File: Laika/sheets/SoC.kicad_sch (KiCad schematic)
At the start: 0 parts

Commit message: Connected USB data in schematic, adjusted Project Architecture
Adjusted the Project Architecture sheet and connected USB between the
Power Connector and SoC sheet. Cleaned up look of the Project
Architecture sheet. Added submodules for Milk V symbols and footprints.
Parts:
- added U1: Milk-V Duo Module, MilkV_Duo:MilkV_DuoModule01_Stamp_88, symbol MilkV_Duo:MilkV_DuoModule01_SG2000
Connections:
- new net +3V3: U1.7 (3V3), U1.8 (3V3)
- new net GND: U1.84 (GND), U1.89 (VCUT), U1.9 (GND)
- new net USB_DM: U1.65 (USB_DM)
- new net USB_DP: U1.66 (USB_DP)
- no-connect marks 0 -> 81
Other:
- note added: "SoC"

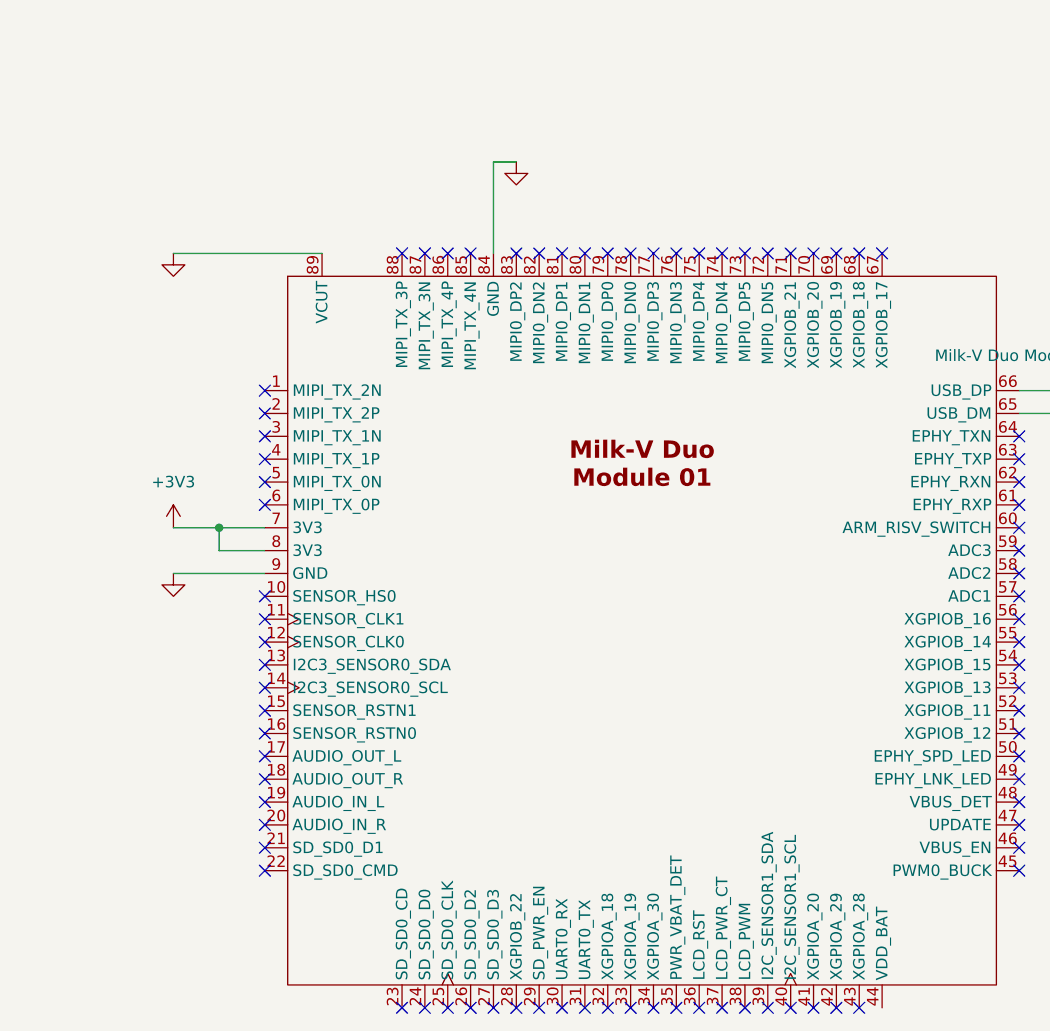
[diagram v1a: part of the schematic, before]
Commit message: Created 3.3V Buck Regulator Circuit
Created schematic for a 3.3V buck regulator. All component selection and
calaculation was performed using TI WEBENCH Power designer, of which the
artifacts are stored in 'calc'. Created Netclasses for PWR and USB.
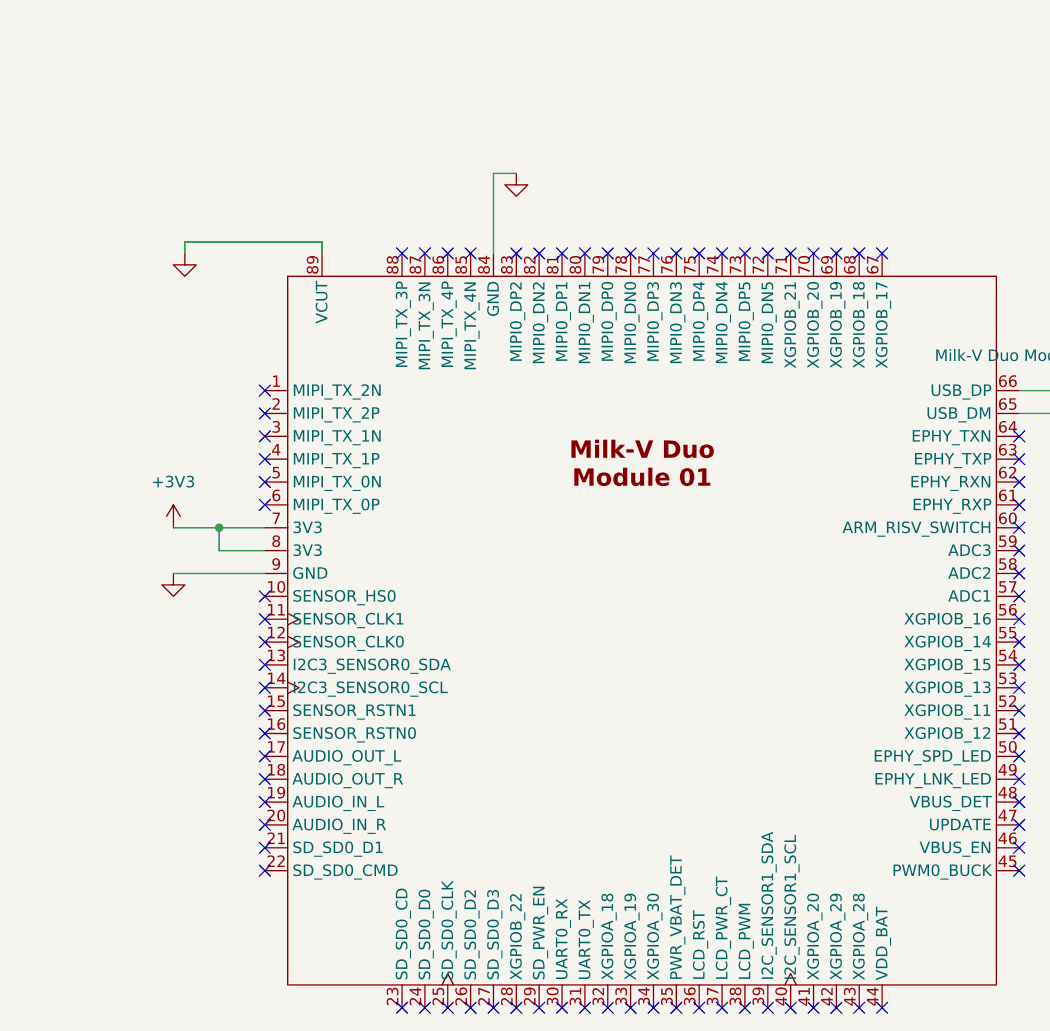
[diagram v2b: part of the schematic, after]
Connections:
- no-connect marks 81 -> 82
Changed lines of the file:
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@@
+	)
+	(no_connect
+		(at 166.37 143.51)
 	)
 	(no_connect
@@
 	(wire
 		(pts
-			(xy 123.19 59.69) (xy 123.19 49.53)
+			(xy 123.19 59.69) (xy 123.19 50.8)
 		)
 		(stroke
@@
 	(wire
 		(pts
-			(xy 123.19 49.53) (xy 125.73 49.53)
+			(xy 123.19 50.8) (xy 125.73 50.8)
 		)
 		(stroke
@@
 	(wire
 		(pts
+			(xy 88.9 58.42) (xy 88.9 59.69)
+		)
+		(stroke
+			(width 0)
+			(type default)
+		)
+	)
+	(wire
+		(pts
+			(xy 104.14 58.42) (xy 104.14 59.69)
+		)
+		(stroke
+			(width 0)
+			(type default)
+		)
+	)
+	(wire
+		(pts
 			(xy 87.63 95.25) (xy 97.79 95.25)
 		)
@@
 	(wire
 		(pts
-			(xy 87.63 59.69) (xy 104.14 59.69)
+			(xy 88.9 58.42) (xy 104.14 58.42)
 		)
 		(stroke
@@
 	(symbol
 		(lib_id "power:GND")
-		(at 125.73 49.53 0)
+		(at 125.73 50.8 0)
 		(unit 1)
 		(exclude_from_sim no)
@@
 		(fields_autoplaced yes)
 		(property "Reference" "#PWR017"
+			(at 125.73 57.15 0)
+			(effects
+				(font
+					(size 1.27 1.27)
+				)
+				(hide yes)
+			)
+		)
+		(property "Value" "GND"
 			(at 125.73 55.88 0)
 			(effects
@@
 			)
 		)
-		(property "Value" "GND"
-			(at 125.73 54.61 0)
-			(effects
-				(font
-					(size 1.27 1.27)
-				)
-				(hide yes)
-			)
-		)
 		(property "Footprint" ""
-			(at 125.73 49.53 0)
+			(at 125.73 50.8 0)
 			(effects
 				(font
@@
 		)
 		(property "Datasheet" ""
-			(at 125.73 49.53 0)
+			(at 125.73 50.8 0)
 			(effects
 				(font
@@
 		)
 		(property "Description" "Power symbol creates a global label with name \"GND\" , ground"
-			(at 125.73 49.53 0)
+			(at 125.73 50.8 0)
 			(effects
 				(font
@@
 			)
 		)
+		(property "JLC Part Type" ""
+			(at 139.7 101.6 0)
+			(effects
+				(font
+					(size 1.27 1.27)
+				)
+				(hide yes)
+			)
+		)
+		(property "Part Number" ""
+			(at 139.7 101.6 0)
+			(effects
+				(font
+					(size 1.27 1.27)
+				)
+				(hide yes)
+			)
+		)
+		(property "Manafacturer" ""
+			(at 139.7 101.6 0)
+			(effects
+				(font
+					(size 1.27 1.27)
+				)
+				(hide yes)
+			)
+		)
 		(pin "21"
 		)
@@
 	(symbol
 		(lib_id "power:GND")
-		(at 87.63 59.69 0)
+		(at 88.9 59.69 0)
 		(unit 1)
 		(exclude_from_sim no)
@@
 		(fields_autoplaced yes)
 		(property "Reference" "#PWR016"
-			(at 87.63 66.04 0)
+			(at 88.9 66.04 0)
 			(effects
 				(font
@@
 		)
 		(property "Value" "GND"
-			(at 87.63 64.77 0)
+			(at 88.9 64.77 0)
 			(effects
 				(font
@@
 		)
 		(property "Footprint" ""
-			(at 87.63 59.69 0)
+			(at 88.9 59.69 0)
 			(effects
 				(font
@@
 		)
 		(property "Datasheet" ""
-			(at 87.63 59.69 0)
+			(at 88.9 59.69 0)
 			(effects
 				(font
@@
 		)
 		(property "Description" "Power symbol creates a global label with name \"GND\" , ground"
-			(at 87.63 59.69 0)
-			(effects
-				(font
+			(at 88.9 59.69 0)
+			(effects
+				(font

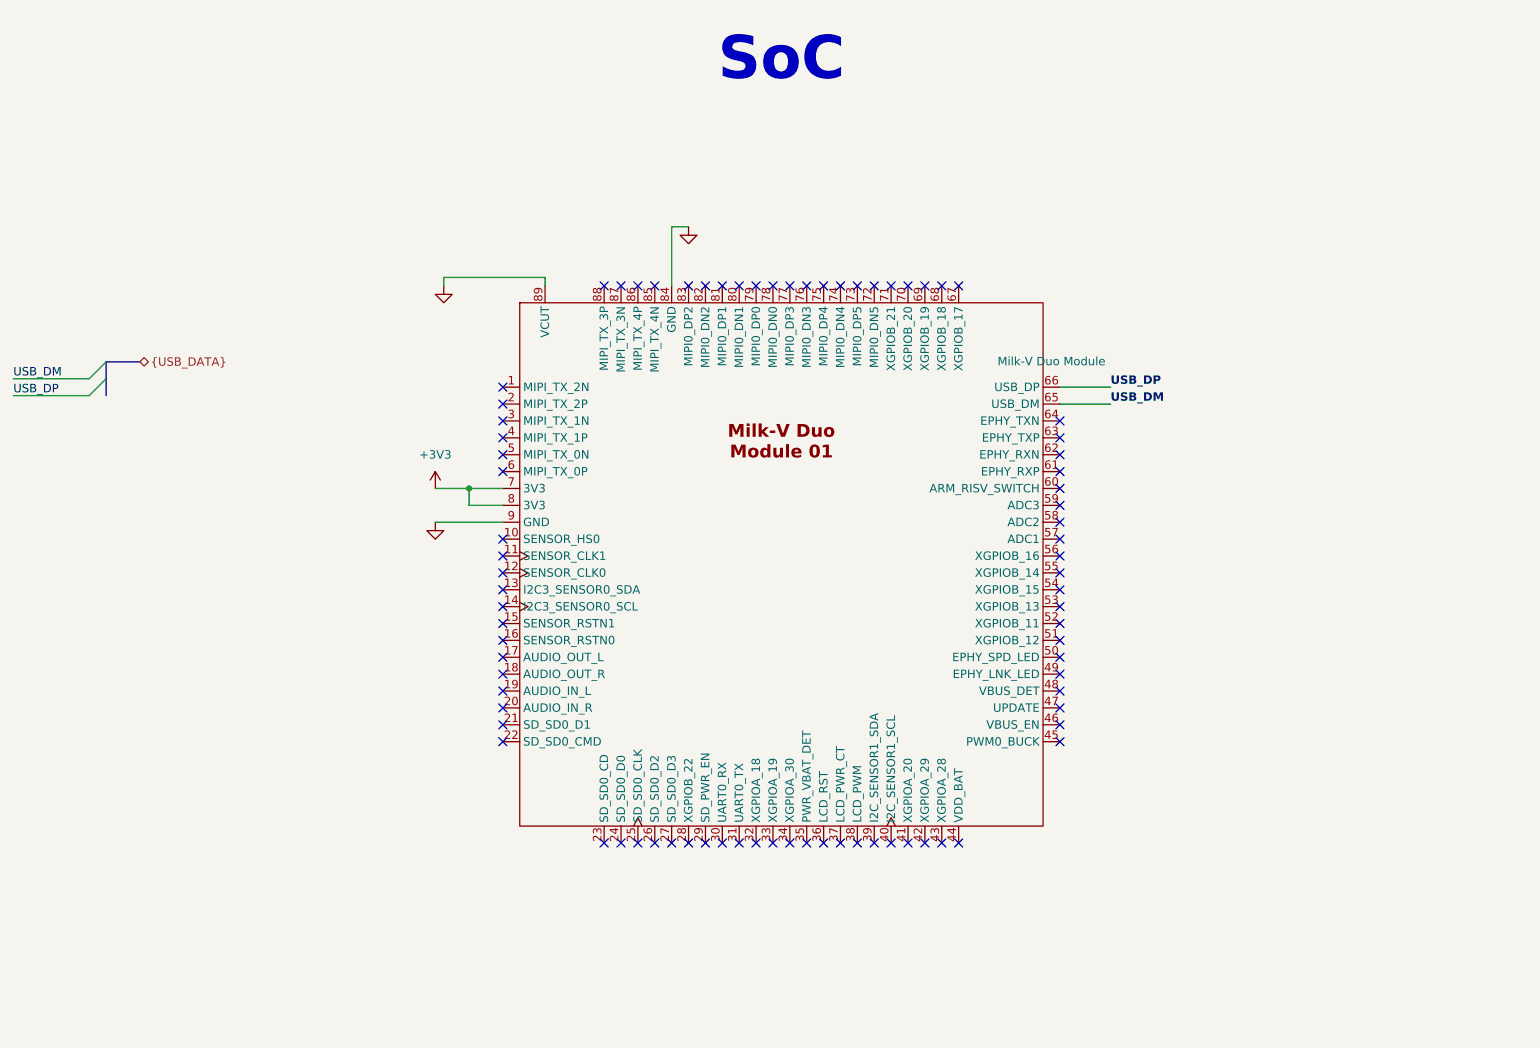
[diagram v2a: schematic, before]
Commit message: Created misc. block
Populated sheet for misc. components. This includes three switches for
SoC bringup (update, reset, arm/risc-v select). Added buzzer and user
led.
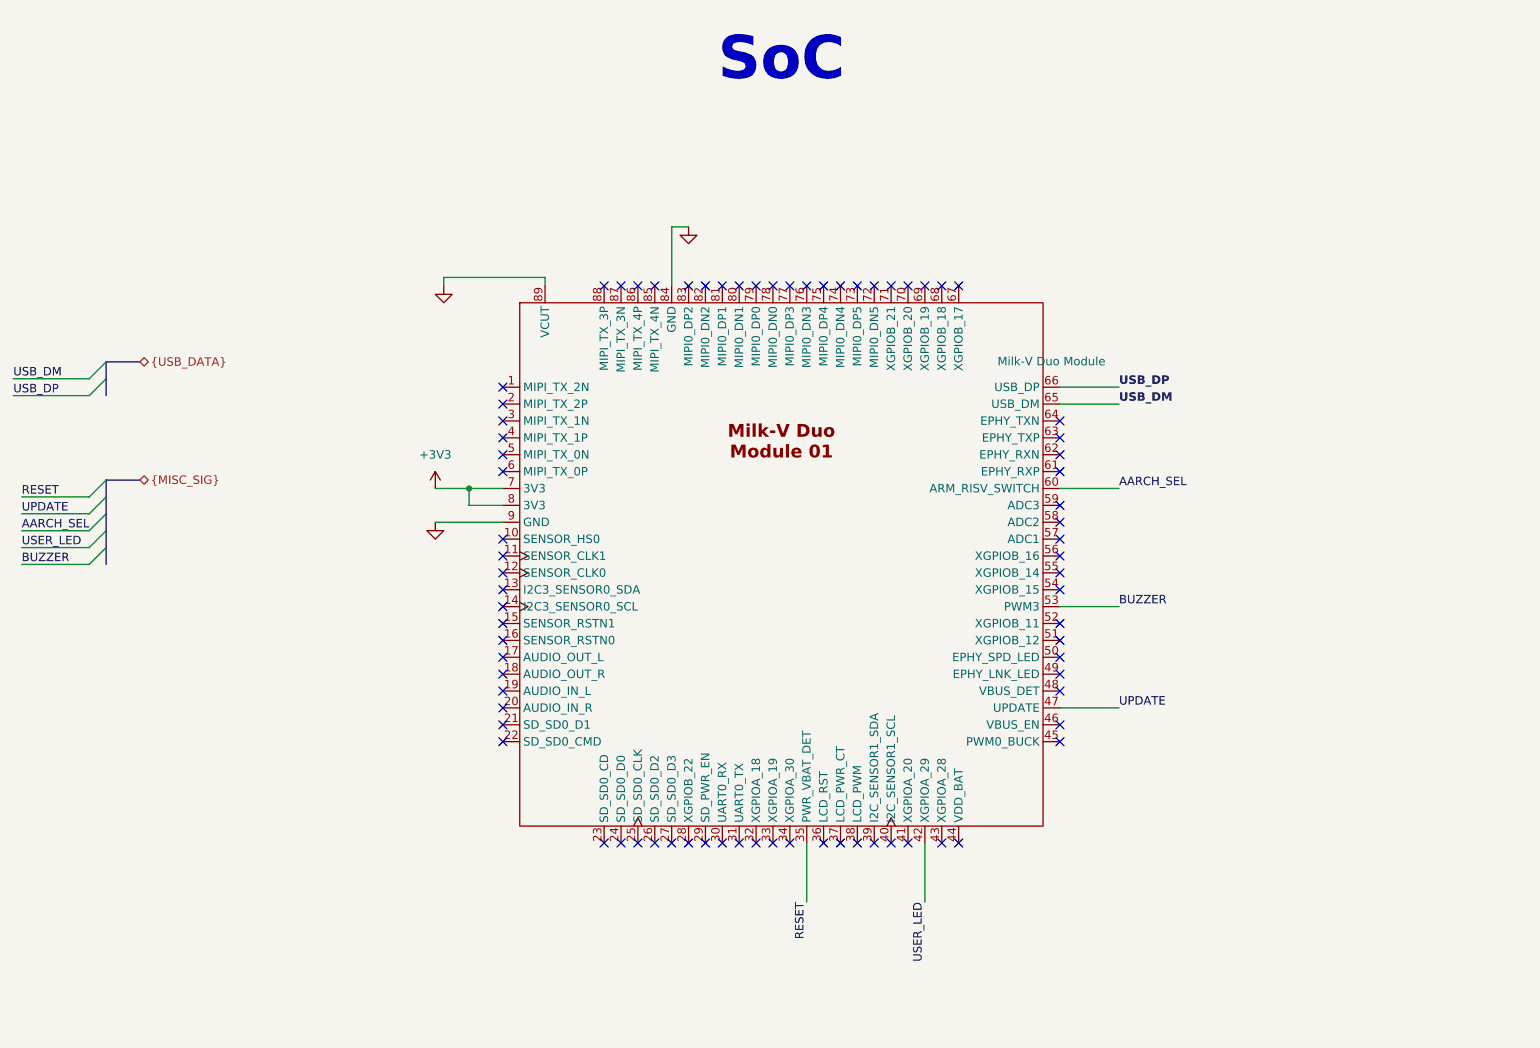
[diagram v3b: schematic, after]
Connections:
- net RESET: now reaches U1.35 (PWR_VBAT_DET)
- net USER_LED: now reaches U1.42 (XGPIOA_29)
- net UPDATE: now reaches U1.47 (UPDATE)
- net BUZZER: now reaches U1.53 (XGPIOB_13)
- net AARCH_SEL: now reaches U1.60 (ARM_RISV_SWITCH)
- no-connect marks 82 -> 77

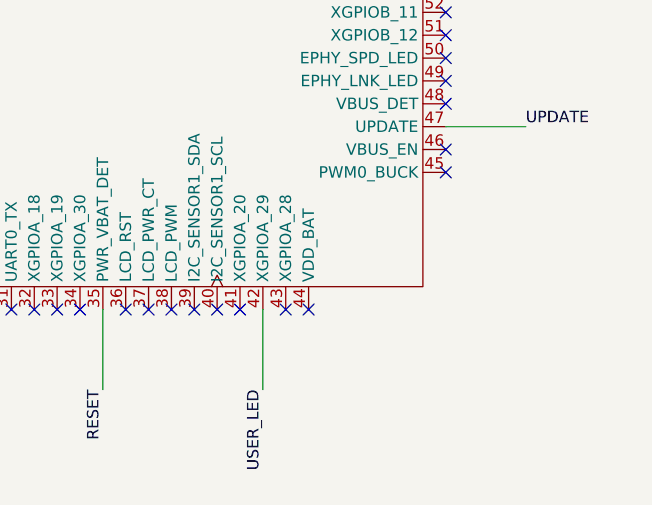
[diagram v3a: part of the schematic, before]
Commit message: Fixed reset block and added VDD_VBAT
Fixed the reset circuit to instead be pulled up to the 3v3 reg using a
voltage divider for 1.8v. RTC power (VDD_BAT) is provided by the 3v3
regulator.
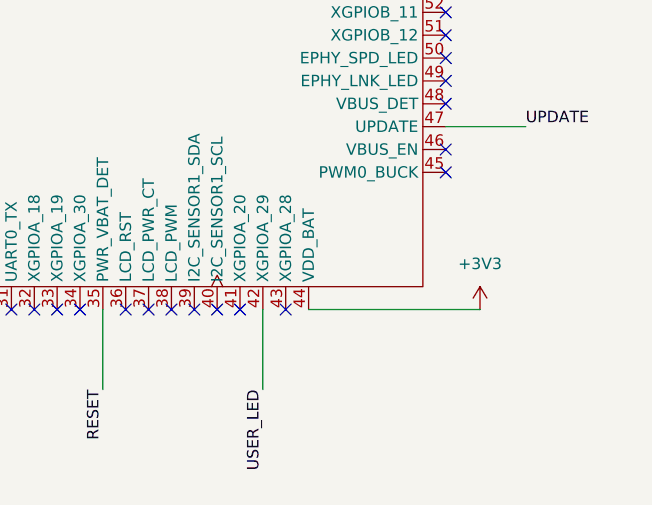
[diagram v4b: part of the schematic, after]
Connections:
- net +3V3: now also U1.44 (VDD_BAT)
- no-connect marks 77 -> 76
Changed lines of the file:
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@@
-	)
-	(no_connect
-		(at 166.37 143.51)
 	)
 	(no_connect
@@
 		(pts
 			(xy 25.4 93.98) (xy 35.56 93.98)
+		)
+		(stroke
+			(width 0)
+			(type default)
+		)
+	)
+	(wire
+		(pts
+			(xy 166.37 143.51) (xy 185.42 143.51)
 		)
 		(stroke
@@
 					(unit 1)
 				)
+			)
+		)
+	)
+	(symbol
+		(lib_id "power:+3V3")
+		(at 185.42 143.51 0)
+		(unit 1)
+		(exclude_from_sim no)
+		(in_bom yes)
+		(on_board yes)
+		(dnp no)
+		(fields_autoplaced yes)
+		(property "Reference" "#PWR043"
+			(at 185.42 147.32 0)
+			(effects
+				(font
+					(size 1.27 1.27)
+				)
+				(hide yes)
+			)
+		)
+		(property "Value" "+3V3"
+			(at 185.42 138.43 0)
+			(effects
+				(font
+					(size 1.27 1.27)
+				)
+			)
+		)
+		(property "Footprint" ""
+			(at 185.42 143.51 0)
+			(effects
+				(font
+					(size 1.27 1.27)
+				)
+				(hide yes)
+			)
+		)
+		(property "Datasheet" ""
+			(at 185.42 143.51 0)
+			(effects
+				(font
+					(size 1.27 1.27)
+				)
+				(hide yes)
+			)
+		)
+		(property "Description" "Power symbol creates a global label with name \"+3V3\""
+			(at 185.42 143.51 0)
+			(effects
+				(font
+					(size 1.27 1.27)
+				)
+				(hide yes)
+			)
+		)
+		(pin "1"
+		)
+		(instances
+			(project "Laika"
+				(path "/57baccbf-5d29-4714-8f2e-7e9f593fcdf8/6c078d98-f795-4bff-ba6d-ace5d579e960/afb454cc-1c16-4ce4-9f1e-961c69cee3bb"
+					(reference "#PWR043")
+					(unit 1)
+				)
